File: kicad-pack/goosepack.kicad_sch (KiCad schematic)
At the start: 72 parts, among them J1 USB_C_Receptacle_USB2.0_16P, J11 Balance, J2 Pack lead, J3 XT30UPB-M, Q2 IRF8736, Q3 IRF8736, U13 BQ7791501, U7 BQ25798

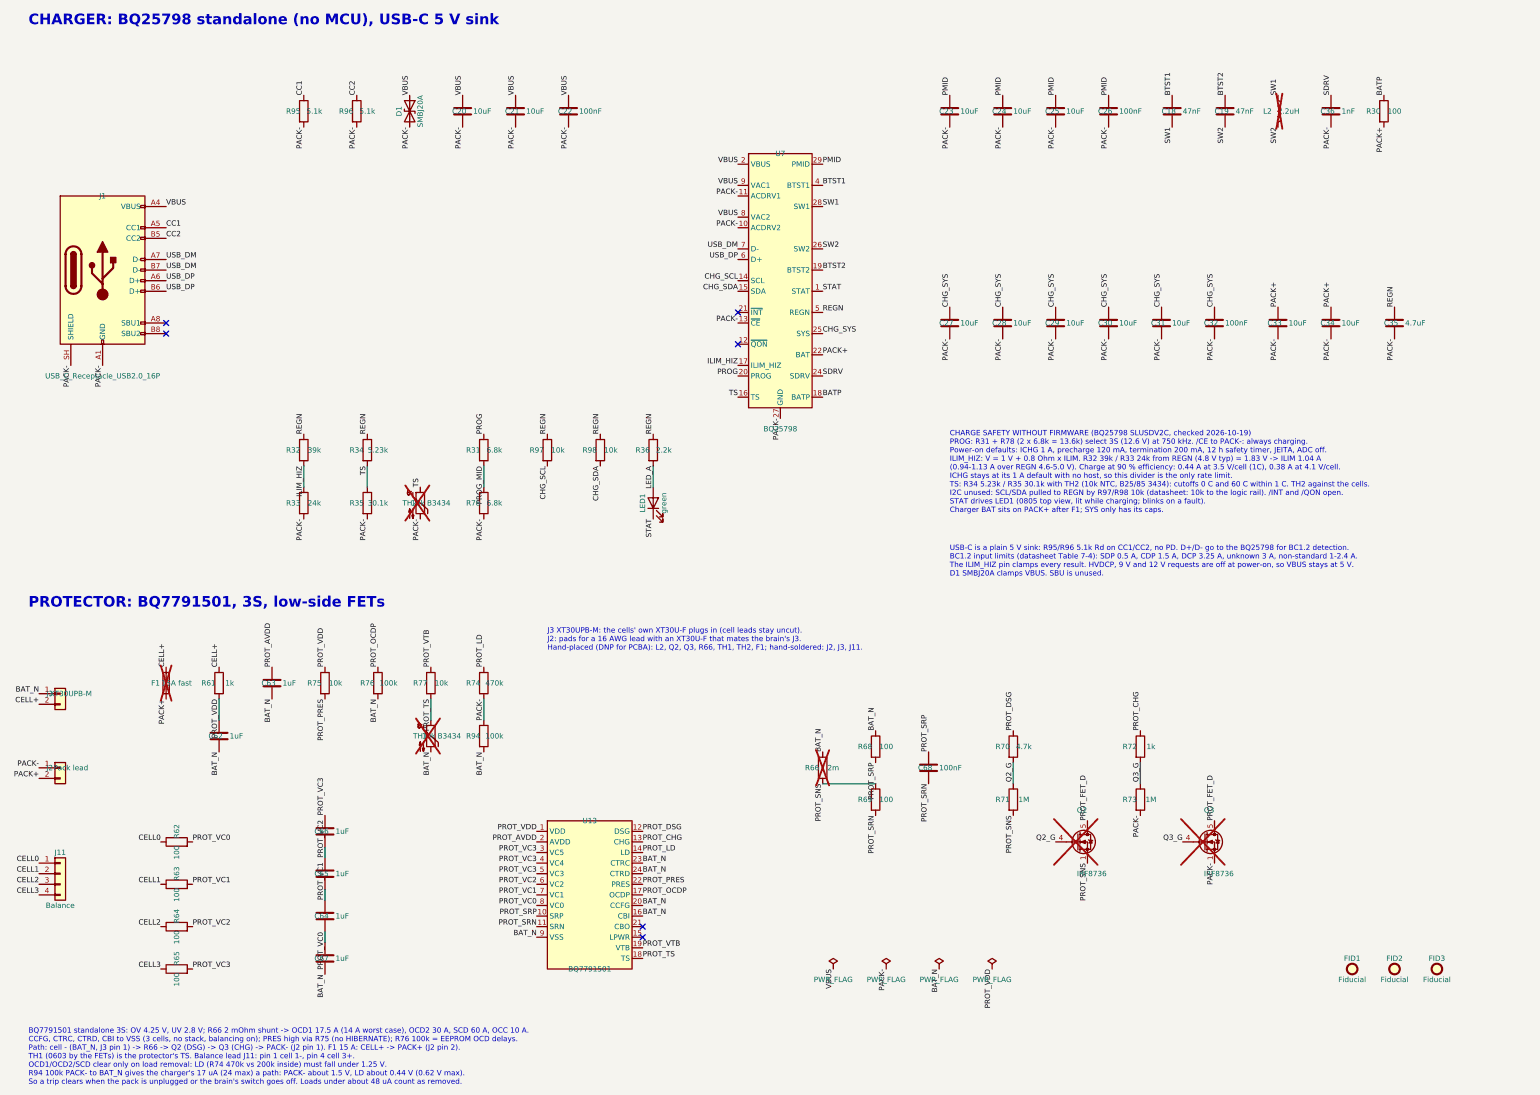
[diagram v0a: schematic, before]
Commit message: Rework the pack charger layout and route the pack board with grid_router
The 3S pack board (kicad-pack/goosepack, 50 x 23 mm, 4 layers) is placed,
routed and finished by scripts alone: tools/place_pack.py compact, then
tools/route_pack.py setup / route / finish, then tools/silk.py pack.

Placement and setup:
- Charger power stage after TI's BQ25798 layout example: U7's power pins
  face L2, SYS and PMID cap rows on F.Cu pours at the pins with the 100 nF
  caps nearest, PGND out between L2's pads to vias under its body.
- Kelvin sense from R66's pad edges to R68/R69 on B.Cu, kept off the fills
  by rule areas.
- Both boot loops laid in setup: C18 under L2 on the SW1 pour, BTST1 by
  B.Cu; C19 over pin 19, SW2 back by In2.
- Setup escapes for U7's crowded corners and J1's CC2/VBUS pads, a stub out
  of C36's SDRV pad; finish drops escape vias the router didn't use.
- grid_router: per-net "router keepout" rule areas (ILIM_HIZ stays 1 mm off
  the SW2 run), via sizes by net class (signals 0.45/0.25, power 0.5/0.3 or
  0.6/0.3), no via within 0.2 mm of an SMD pad.
- ROUTE_ORDER /STAT,/CHG_SYS,/BTST1,/PROG, then the router's own order.

DRC with zones refilled: 0 errors, 0 unconnected, schematic parity clean.
A fresh-eyes review scored the layout 3.5/5 with no blockers.

Parts: C18/C19 now 0402 (C192385, extended), D1 now SMBJ15A (C19077569,
24.4 V clamp under the BQ25798's 30 V VBUS maximum). The pack is ordered
with ENIG. Silk gets polarity labels at both pigtails and the balance pins.

Also adds the route_loop.py / route_llm.py / escape.py diagnose-and-retry
tools that found the route order.

Co-Authored-By: Claude Opus 5.5 <noreply@anthropic.com>
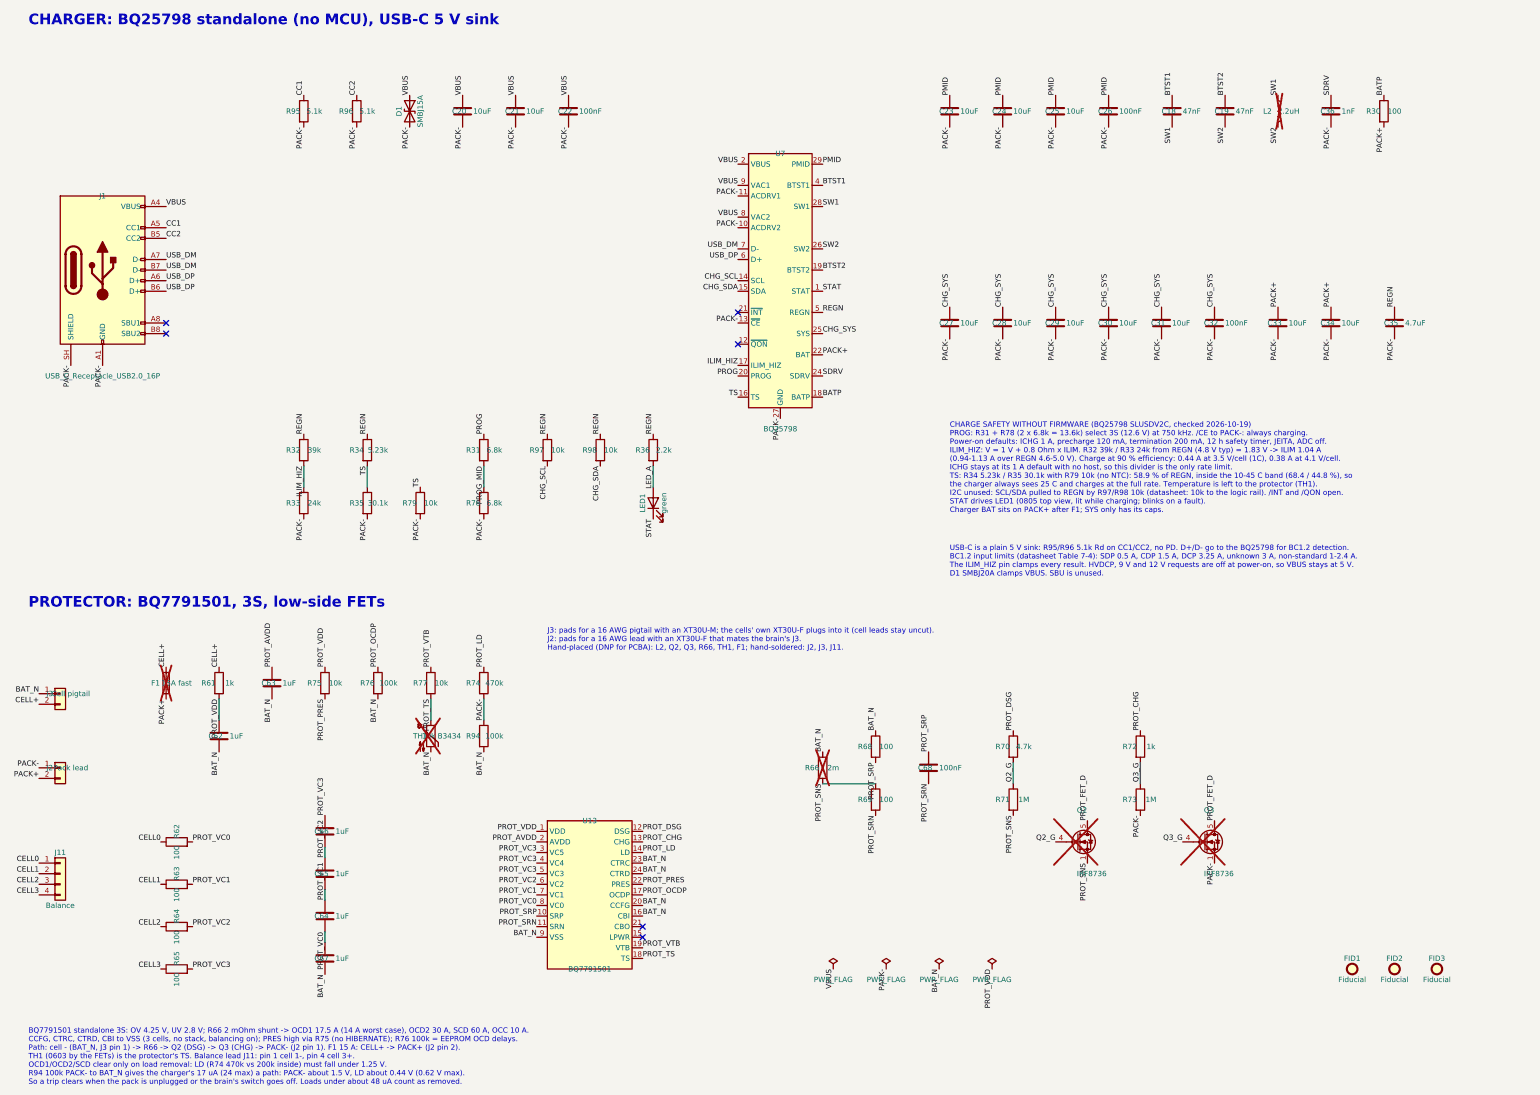
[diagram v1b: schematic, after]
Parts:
- C18, C19: footprint Capacitor_SMD:C_0603_1608Metric -> Capacitor_SMD:C_0402_1005Metric; LCSC Part # C1622 -> C192385; MPN 0603B473K500NT -> 0402B473K160NT
- D1: value SMBJ20A -> SMBJ15A; LCSC Part # C19077575 -> C19077569; MPN SMBJ20A -> SMBJ15A
- J2: footprint hexy:XT30_SolderPads_1x02_P5.00mm -> Connector_Wire:SolderWire-1.5sqmm_1x02_P6mm_D1.7mm_OD3mm
- J3: value XT30UPB-M -> Cell pigtail; footprint hexy:AMASS_XT30UPB-M_1x02_P5.0mm_Vertical_EasyEDA3D -> Connector_Wire:SolderWire-1.5sqmm_1x02_P6mm_D1.7mm_OD3mm; LCSC Part # C428721 -> C99101; MPN XT30UPB-M -> XT30U-M
- R79: renamed from TH2; value 10k B3434 -> 10k; symbol Device:Thermistor_NTC -> Device:R; LCSC Part # C13564 -> C25804; MPN NCP18XH103F03RB -> 0603WAF1002T5E; Manufacturer Murata -> UNI-ROYAL; now fitted
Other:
- note added: "J3: pads for a 16 AWG pigtail with an XT30U-M; the cells' own XT30U-F plugs into it (cell leads stay uncut). J2: pads for a 16 AWG lead with an XT30U-F that mates the brain's J3. Hand-placed (DNP for PCBA): L2, Q2, Q3, R66, TH1, F1; hand-soldered: J2, J3, J11."
- note removed: "J3 XT30UPB-M: the cells' own XT30U-F plugs in (cell leads stay uncut). J2: pads for a 16 AWG lead with an XT30U-F that mates the brain's J3. Hand-placed (DNP for PCBA): L2, Q2, Q3, R66, TH1, TH2, F1; hand-soldered: J2, J3, J11."
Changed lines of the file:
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@@
 			)
 		)
-		(property "Value" "SMBJ20A"
+		(property "Value" "SMBJ15A"
 			(at 116.84 50.8 0)
 			(show_name no)
@@
 			)
 		)
-		(property "MPN" "SMBJ20A"
+		(property "MPN" "SMBJ15A"
 			(at 114.3 50.8 0)
 			(effects
@@
 			)
 		)
-		(property "LCSC Part #" "C19077575"
+		(property "LCSC Part #" "C19077569"
 			(at 114.3 50.8 0)
 			(effects
@@
 	)
 	(symbol
-		(lib_id "Device:Thermistor_NTC")
+		(lib_id "Device:R")
 		(at 116.84 144.78 0)
 		(unit 1)
@@
 		(on_board yes)
 		(in_pos_files yes)
-		(dnp yes)
-		(property "Reference" "TH2"
+		(dnp no)
+		(property "Reference" "R79"
 			(at 114.3 144.78 0)
 			(show_name no)
@@
 			)
 		)
-		(property "Value" "10k B3434"
+		(property "Value" "10k"
 			(at 119.38 144.78 0)
 			(show_name no)
@@
 			)
 		)
-		(property "Description" "Temperature dependent resistor, negative temperature coefficient"
+		(property "Description" "Resistor"
 			(at 116.84 144.78 0)
 			(hide yes)
@@
 			)
 		)
-		(property "MPN" "NCP18XH103F03RB"
+		(property "MPN" "0603WAF1002T5E"
 			(at 116.84 144.78 0)
 			(effects
@@
 			)
 		)
-		(property "Manufacturer" "Murata"
+		(property "Manufacturer" "UNI-ROYAL"
 			(at 116.84 144.78 0)
 			(effects
@@
 			)
 		)
-		(property "LCSC Part #" "C13564"
+		(property "LCSC Part #" "C25804"
 			(at 116.84 144.78 0)
 			(effects
@@
 			(project "goosepack"
 				(path "/b039c4cd-30f0-48b1-bce5-22fee9821a58"
-					(reference "TH2")
+					(reference "R79")
 					(unit 1)
 				)
@@
 			)
 		)
-		(property "Footprint" "Capacitor_SMD:C_0603_1608Metric"
+		(property "Footprint" "Capacitor_SMD:C_0402_1005Metric"
 			(at 298.145 46.99 0)
 			(hide yes)
@@
 			)
 		)
-		(property "MPN" "0603B473K500NT"
+		(property "MPN" "0402B473K160NT"
 			(at 297.18 50.8 0)
 			(effects
@@
 			)
 		)
-		(property "LCSC Part #" "C1622"
+		(property "LCSC Part #" "C192385"
 			(at 297.18 50.8 0)
 			(effects
@@
 			)
 		)
-		(property "Footprint" "Capacitor_SMD:C_0603_1608Metric"
+		(property "Footprint" "Capacitor_SMD:C_0402_1005Metric"
 			(at 310.845 46.99 0)
 			(hide yes)
@@
 			)
 		)
-		(property "MPN" "0603B473K500NT"
+		(property "MPN" "0402B473K160NT"
 			(at 309.88 50.8 0)
 			(effects
@@
 			)
 		)
-		(property "LCSC Part #" "C1622"
+		(property "LCSC Part #" "C192385"
 			(at 309.88 50.8 0)
 			(effects
@@
 			)
 		)
-		(property "Value" "XT30UPB-M"
+		(property "Value" "Cell pigtail"
 			(at 33.02 190.5 0)
 			(show_name no)
@@
 			)
 		)
-		(property "Footprint" "hexy:AMASS_XT30UPB-M_1x02_P5.0mm_Vertical_EasyEDA3D"
+		(property "Footprint" "Connector_Wire:SolderWire-1.5sqmm_1x02_P6mm_D1.7mm_OD3mm"
 			(at 30.48 190.5 0)
 			(hide yes)
@@
 			)
 		)
-		(property "MPN" "XT30UPB-M"
+		(property "MPN" "XT30U-M"
 			(at 30.48 190.5 0)
 			(effects
@@
 			)
 		)
-		(property "LCSC Part #" "C428721"
+		(property "LCSC Part #" "C99101"
 			(at 30.48 190.5 0)
 			(effects
@@
 			)
 		)
-		(property "Footprint" "hexy:XT30_SolderPads_1x02_P5.00mm"
+		(property "Footprint" "Connector_Wire:SolderWire-1.5sqmm_1x02_P6mm_D1.7mm_OD3mm"
 			(at 30.48 208.28 0)
 			(hide yes)
@@
 		)
 	)
-	(text "CHARGE SAFETY WITHOUT FIRMWARE (BQ25798 SLUSDV2C, checked 2026-10-19)\nPROG: R31 + R78 (2 x 6.8k = 13.6k) select 3S (12.6 V) at 750 kHz. /CE to PACK-: always charging.\nPower-on defaults: ICHG 1 A, precharge 120 mA, termination 200 mA, 12 h safety timer, JEITA, ADC off.\nILIM_HIZ: V = 1 V + 0.8 Ohm x ILIM. R32 39k / R33 24k from REGN (4.8 V typ) = 1.83 V -> ILIM 1.04 A\n(0.94-1.13 A over REGN 4.6-5.0 V). Charge at 90 % efficiency: 0.44 A at 3.5 V/cell (1C), 0.38 A at 4.1 V/cell.\nICHG stays at its 1 A default with no host, so this divider is the only rate limit.\nTS: R34 5.23k / R35 30.1k with TH2 (10k NTC, B25/85 3434): cutoffs 0 C and 60 C within 1 C. TH2 against the cells.\nI2C unused: SCL/SDA pulled to REGN by R97/R98 10k (datasheet: 10k to the logic rail). /INT and /QON open.\nSTAT drives LED1 (0805 top view, lit while charging; blinks on a fault).\nCharger BAT sits on PACK+ after F1; SYS only has its caps."
+	(text "CHARGE SAFETY WITHOUT FIRMWARE (BQ25798 SLUSDV2C, checked 2026-10-19)\nPROG: R31 + R78 (2 x 6.8k = 13.6k) select 3S (12.6 V) at 750 kHz. /CE to PACK-: always charging.\nPower-on defaults: ICHG 1 A, precharge 120 mA, termination 200 mA, 12 h safety timer, JEITA, ADC off.\nILIM_HIZ: V = 1 V + 0.8 Ohm x ILIM. R32 39k / R33 24k from REGN (4.8 V typ) = 1.83 V -> ILIM 1.04 A\n(0.94-1.13 A over REGN 4.6-5.0 V). Charge at 90 % efficiency: 0.44 A at 3.5 V/cell (1C), 0.38 A at 4.1 V/cell.\nICHG stays at its 1 A default with no host, so this divider is the only rate limit.\nTS: R34 5.23k / R35 30.1k with R79 10k (no NTC): 58.9 % of REGN, inside the 10-45 C band (68.4 / 44.8 %), so\nthe charger always sees 25 C and charges at the full rate. Temperature is left to the protector (TH1).\nI2C unused: SCL/SDA pulled to REGN by R97/R98 10k (datasheet: 10k to the logic rail). /INT and /QON open.\nSTAT drives LED1 (0805 top view, lit while charging; blinks on a fault).\nCharger BAT sits on PACK+ after F1; SYS only has its caps."
 		(exclude_from_sim no)
 		(at 243.84 147.32 0)
@@
 		)
 	)
-	(text "J3 XT30UPB-M: the cells' own XT30U-F plugs in (cell leads stay uncut).\nJ2: pads for a 16 AWG lead with an XT30U-F that mates the brain's J3.\nHand-placed (DNP for PCBA): L2, Q2, Q3, R66, TH1, TH2, F1; hand-soldered: J2, J3, J11."
+	(text "J3: pads for a 16 AWG pigtail with an XT30U-M; the cells' own XT30U-F plugs into it (cell leads stay uncut).\nJ2: pads for a 16 AWG lead with an XT30U-F that mates the brain's J3.\nHand-placed (DNP for PCBA): L2, Q2, Q3, R66, TH1, F1; hand-soldered: J2, J3, J11."
 		(exclude_from_sim no)
 		(at 147.32 180.34 0)

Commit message: Have JLC place every 3S pack SMD part and document the pack process
- Clear DNP on L2, Q2, Q3, R66, TH1 and F1 (schematic and board); PARTS.md
  and README updated.
- Route with 0.3 mm via drills, extend ROUTE_ORDER, stage finish; lead-free
  HASL in the stackup.
- Add docs/3s-pack-process.md, the placement-to-JLC-order recipe, linked
  from the README, and the brain/pack side-by-side render.

Co-Authored-By: Claude Opus 5.5 <noreply@anthropic.com>
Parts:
- F1, L2, Q2, Q3, R66, TH1: now fitted
- R34: LCSC Part # C25907 -> C11631; MPN 0402WGF5231TCE -> RTT025231FTH; Manufacturer UNI-ROYAL -> RALEC
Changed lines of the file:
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@@
 			)
 		)
-		(property "MPN" "0402WGF5231TCE"
+		(property "MPN" "RTT025231FTH"
 			(at 104.14 132.08 0)
 			(effects
@@
 			)
 		)
-		(property "Manufacturer" "UNI-ROYAL"
+		(property "Manufacturer" "RALEC"
 			(at 104.14 132.08 0)
 			(effects
@@
 			)
 		)
-		(property "LCSC Part #" "C25907"
+		(property "LCSC Part #" "C11631"
 			(at 104.14 132.08 0)
 			(effects
@@
 		(on_board yes)
 		(in_pos_files yes)
-		(dnp yes)
+		(dnp no)
 		(property "Reference" "L2"
 			(at 320.04 50.8 0)
@@
 		(on_board yes)
 		(in_pos_files yes)
-		(dnp yes)
+		(dnp no)
 		(property "Reference" "F1"
 			(at 53.34 187.96 0)
@@
 		(on_board yes)
 		(in_pos_files yes)
-		(dnp yes)
+		(dnp no)
 		(property "Reference" "TH1"
 			(at 116.84 200.66 0)
@@
 		(on_board yes)
 		(in_pos_files yes)
-		(dnp yes)
+		(dnp no)
 		(property "Reference" "R66"
 			(at 210.82 208.28 0)
@@
 		(on_board yes)
 		(in_pos_files yes)
-		(dnp yes)
+		(dnp no)
 		(property "Reference" "Q2"
 			(at 274.32 218.44 0)
@@
 		(on_board yes)
 		(in_pos_files yes)
-		(dnp yes)
+		(dnp no)
 		(property "Reference" "Q3"
 			(at 304.8 218.44 0)
